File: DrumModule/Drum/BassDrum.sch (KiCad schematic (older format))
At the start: 35 parts, among them J1 Barrel_Jack_Switch, J2 Barrel_Jack_Switch, Q1 MMBT3904, U1 74HC74, U3 LM2904DR, U4 LM2904DR, U5 LM2904DR

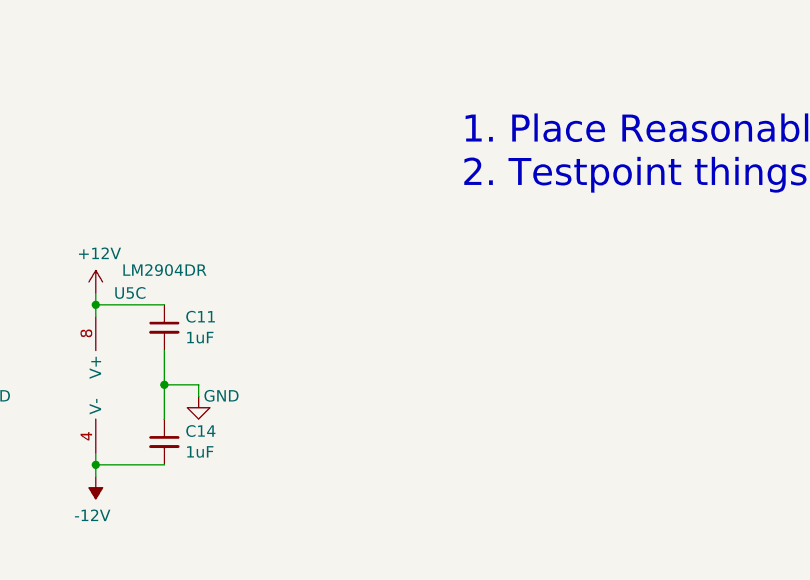
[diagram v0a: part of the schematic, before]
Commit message: Organized layout of drum, should be ready for routing.
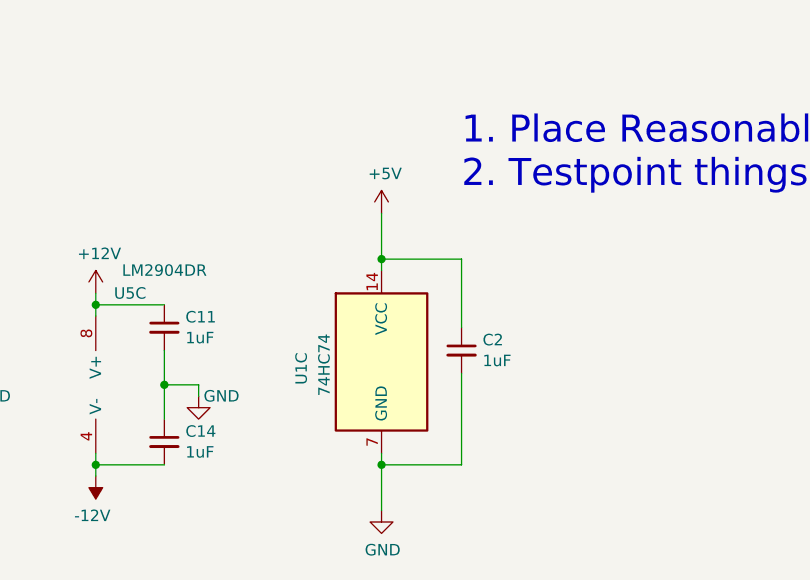
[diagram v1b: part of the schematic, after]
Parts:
- added C2: 1uF, Capacitor_SMD:C_0805_2012Metric, symbol Device:C_Small
- added unit 3 of U1
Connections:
- net +5V: now also C2.1, U1.14 (VCC)
- net GND: now also C2.2, U1.7 (GND)
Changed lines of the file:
@@
 Text Notes 4900 5950 0    118  ~ 0
 1. Place Reasonable values for HPF/LPF.\n2. Testpoint things.
+$Comp
+L 74xx:74HC74 U?
+U 3 1 5C9E2140
+P 4550 6700
+AR Path="/5C9E2140" Ref="U?"  Part="3"
+AR Path="/5C9E40A5/5C9E2140" Ref="U1"  Part="3"
+F 0 "U1" V 4200 6600 50  0000 L CNN
+F 1 "74HC74" V 4300 6550 50  0000 L CNN
+F 2 "Package_SO:SOIC-14_3.9x8.7mm_P1.27mm" H 4550 6700 50  0001 C CNN
+F 3 "74xx/74hc_hct74.pdf" H 4550 6700 50  0001 C CNN
+	3    4550 6700
+	1    0    0    -1
+$EndComp
+Wire Wire Line
+	4550 6300 4550 6250
+Wire Wire Line
+	4550 7100 4550 7150
+$Comp
+L power:GND #PWR?
+U 1 1 5C9E2149
+P 4550 7350
+AR Path="/5C9E2149" Ref="#PWR?"  Part="1"
+AR Path="/5C9E40A5/5C9E2149" Ref="#PWR011"  Part="1"
+F 0 "#PWR011" H 4550 7100 50  0001 C CNN
+F 1 "GND" H 4555 7177 50  0000 C CNN
+F 2 "" H 4550 7350 50  0001 C CNN
+F 3 "" H 4550 7350 50  0001 C CNN
+	1    4550 7350
+	1    0    0    -1
+$EndComp
+Wire Wire Line
+	4550 7150 4900 7150
+Connection ~ 4550 7150
+Wire Wire Line
+	4550 7150 4550 7350
+Wire Wire Line
+	4900 6250 4550 6250
+Connection ~ 4550 6250
+Wire Wire Line
+	4550 6250 4550 6050
+$Comp
+L power:+5V #PWR?
+U 1 1 5C9E2155
+P 4550 6050
+AR Path="/5C9E2155" Ref="#PWR?"  Part="1"
+AR Path="/5C9E40A5/5C9E2155" Ref="#PWR010"  Part="1"
+F 0 "#PWR010" H 4550 5900 50  0001 C CNN
+F 1 "+5V" H 4565 6223 50  0000 C CNN
+F 2 "" H 4550 6050 50  0001 C CNN
+F 3 "" H 4550 6050 50  0001 C CNN
+	1    4550 6050
+	1    0    0    -1
+$EndComp
+$Comp
+L Device:C_Small C?
+U 1 1 5C9E215B
+P 4900 6650
+AR Path="/5C9E215B" Ref="C?"  Part="1"
+AR Path="/5C9E40A5/5C9E215B" Ref="C2"  Part="1"
+F 0 "C2" H 4992 6696 50  0000 L CNN
+F 1 "1uF" H 4992 6605 50  0000 L CNN
+F 2 "Capacitor_SMD:C_0805_2012Metric" H 4900 6650 50  0001 C CNN
+F 3 "~" H 4900 6650 50  0001 C CNN
+	1    4900 6650
+	1    0    0    -1
+$EndComp
+Wire Wire Line
+	4900 6250 4900 6550
+Wire Wire Line
+	4900 6750 4900 7150
 $EndSCHEMATC

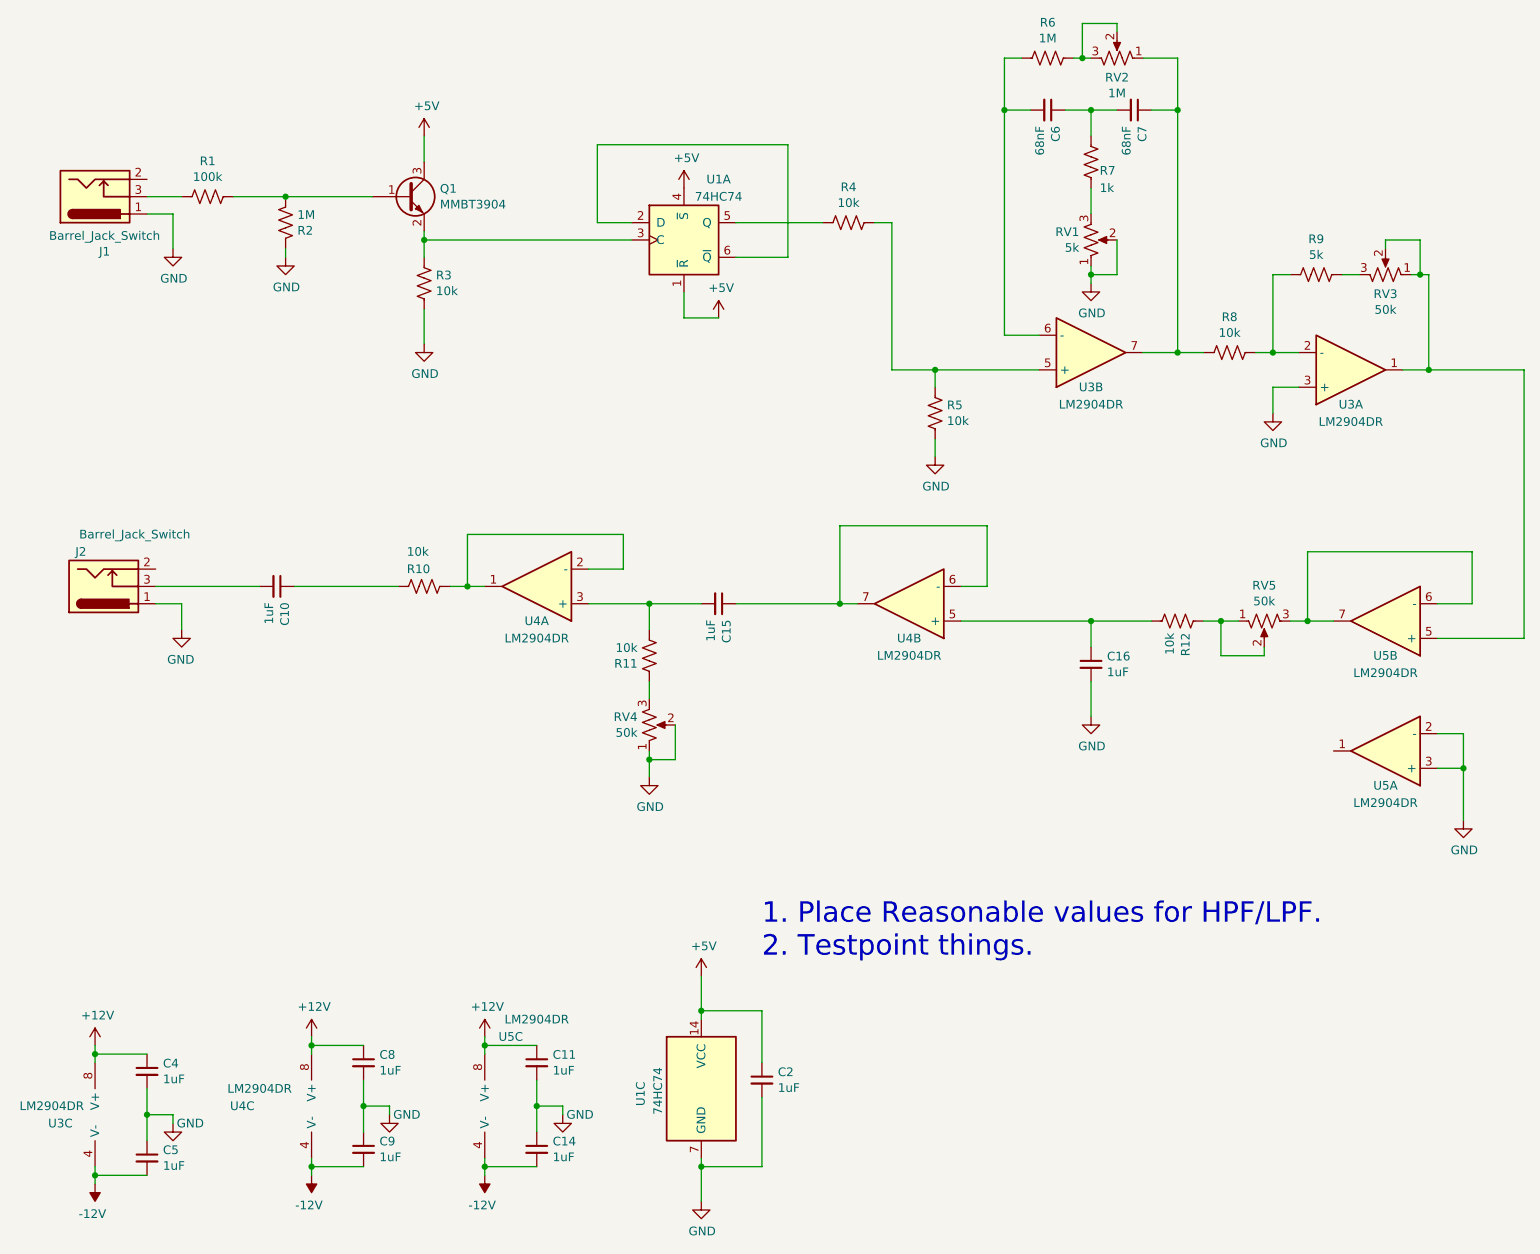
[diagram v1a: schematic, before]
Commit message: locked in filter values
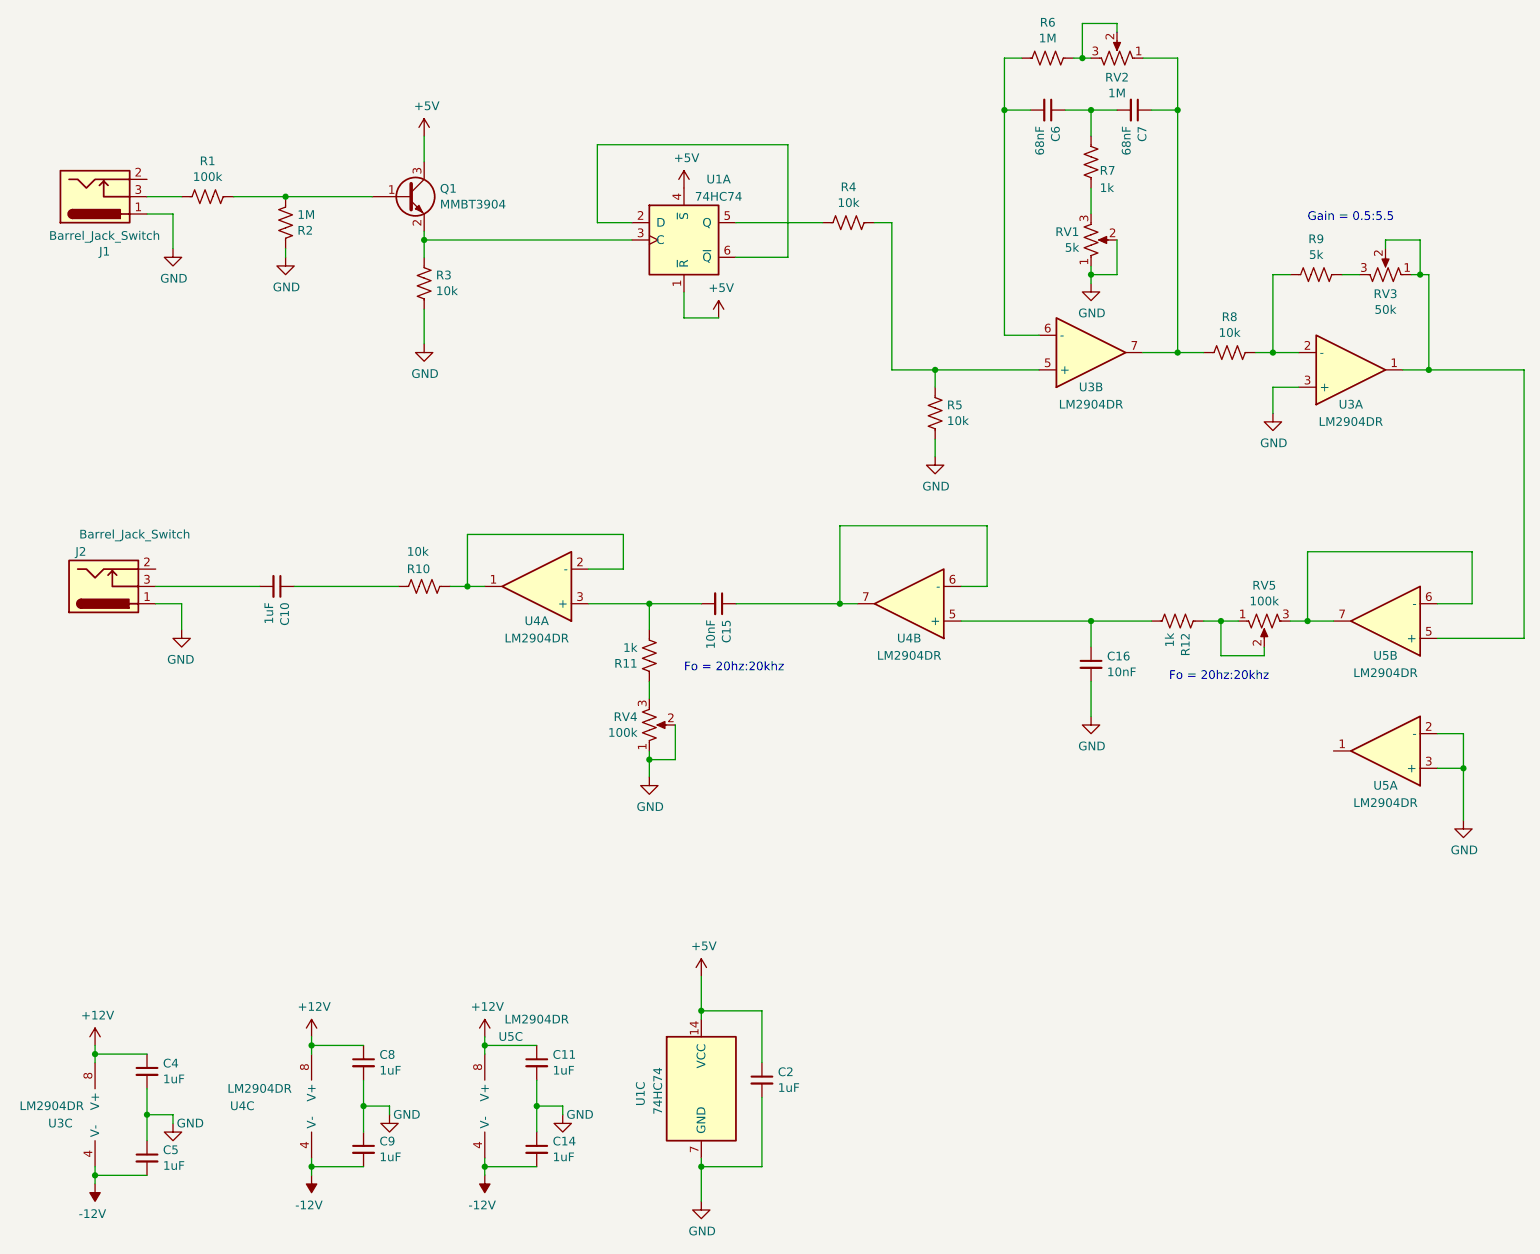
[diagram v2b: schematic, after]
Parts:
- C15, C16: value 1uF -> 10nF
- R11, R12: value 10k -> 1k
- RV4, RV5: value 50k -> 100k
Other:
- note added: "Fo = 20hz:20khz"
- note added: "Gain = 0.5:5.5"
- note removed: "1. Place Reasonable values for HPF/LPF.\n2. Testpoint things."
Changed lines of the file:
@@
 P 7300 4000
 F 0 "R12" H 7368 4046 50  0000 L CNN
-F 1 "10k" H 7368 3955 50  0000 L CNN
+F 1 "1k" H 7368 3955 50  0000 L CNN
 F 2 "Resistor_SMD:R_0805_2012Metric" V 7340 3990 50  0001 C CNN
 F 3 "~" H 7300 4000 50  0001 C CNN
@@
 AR Path="/5C9E40A5/5CA38E3F" Ref="C16"  Part="1"
 F 0 "C16" H 6892 4296 50  0000 L CNN
-F 1 "1uF" H 6892 4205 50  0000 L CNN
+F 1 "10nF" H 6892 4205 50  0000 L CNN
 F 2 "Capacitor_SMD:C_0805_2012Metric" H 6800 4250 50  0001 C CNN
 F 3 "~" H 6800 4250 50  0001 C CNN
@@
 P 4250 4200
 F 0 "R11" H 4318 4246 50  0000 L CNN
-F 1 "10k" H 4318 4155 50  0000 L CNN
+F 1 "1k" H 4318 4155 50  0000 L CNN
 F 2 "Resistor_SMD:R_0805_2012Metric" V 4290 4190 50  0001 C CNN
 F 3 "~" H 4250 4200 50  0001 C CNN
@@
 AR Path="/5C9E40A5/5CA4B038" Ref="C15"  Part="1"
 F 0 "C15" H 4742 3946 50  0000 L CNN
-F 1 "1uF" H 4742 3855 50  0000 L CNN
+F 1 "10nF" H 4742 3855 50  0000 L CNN
 F 2 "Capacitor_SMD:C_0805_2012Metric" H 4650 3900 50  0001 C CNN
 F 3 "~" H 4650 3900 50  0001 C CNN
@@
 P 4250 4600
 F 0 "RV4" H 4182 4554 50  0000 R CNN
-F 1 "50k" H 4182 4645 50  0000 R CNN
+F 1 "100k" H 4182 4645 50  0000 R CNN
 F 2 "Eurocad:Alpha9mmPot" H 4250 4600 50  0001 C CNN
 F 3 "~" H 4250 4600 50  0001 C CNN
@@
 P 7800 4000
 F 0 "RV5" V 7595 4000 50  0000 C CNN
-F 1 "50k" V 7686 4000 50  0000 C CNN
+F 1 "100k" V 7686 4000 50  0000 C CNN
 F 2 "Eurocad:Alpha9mmPot" H 7800 4000 50  0001 C CNN
 F 3 "~" H 7800 4000 50  0001 C CNN
@@
 	3300 7200 3300 7150
 Connection ~ 3300 7150
-Text Notes 4900 5950 0    118  ~ 0
-1. Place Reasonable values for HPF/LPF.\n2. Testpoint things.
 $Comp
 L 74xx:74HC74 U?
@@
 Wire Wire Line
 	4900 6750 4900 7150
+Text Notes 8050 1700 0    50   ~ 0
+Gain = 0.5:5.5
+Text Notes 7250 4350 0    50   ~ 0
+Fo = 20hz:20khz
+Text Notes 4450 4300 0    50   ~ 0
+Fo = 20hz:20khz
 $EndSCHEMATC

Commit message: Forgot to save
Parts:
- RV1: value 5k -> 1k
- RV2: value 1M -> 100k
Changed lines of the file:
@@
 P 6800 1800
 F 0 "RV1" H 6732 1754 50  0000 R CNN
-F 1 "5k" H 6732 1845 50  0000 R CNN
+F 1 "1k" H 6732 1845 50  0000 R CNN
 F 2 "Eurocad:Alpha9mmPot" H 6800 1800 50  0001 C CNN
 F 3 "~" H 6800 1800 50  0001 C CNN
@@
 P 6950 750
 F 0 "RV2" V 6838 750 50  0000 C CNN
-F 1 "1M" V 6747 750 50  0000 C CNN
+F 1 "100k" V 6747 750 50  0000 C CNN
 F 2 "Eurocad:Alpha9mmPot" H 6950 750 50  0001 C CNN
 F 3 "~" H 6950 750 50  0001 C CNN

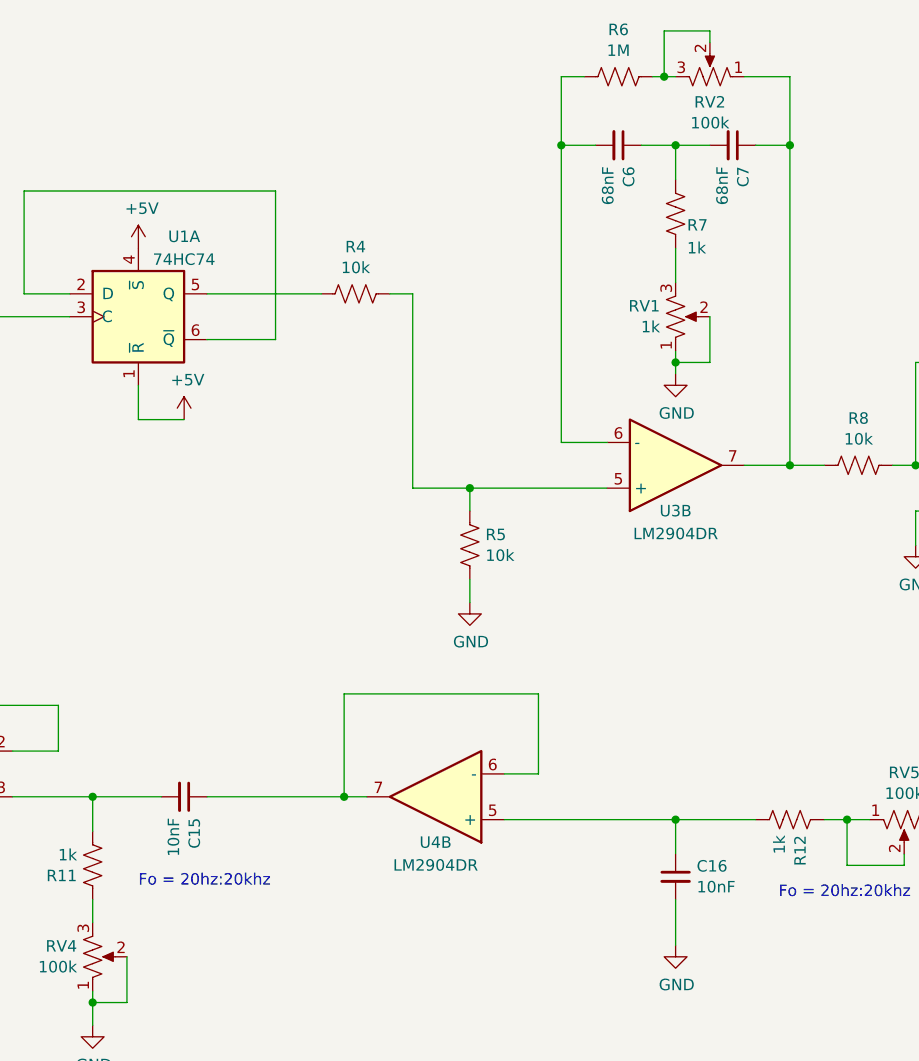
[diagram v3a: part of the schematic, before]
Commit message: Updated parts for the Bob bass
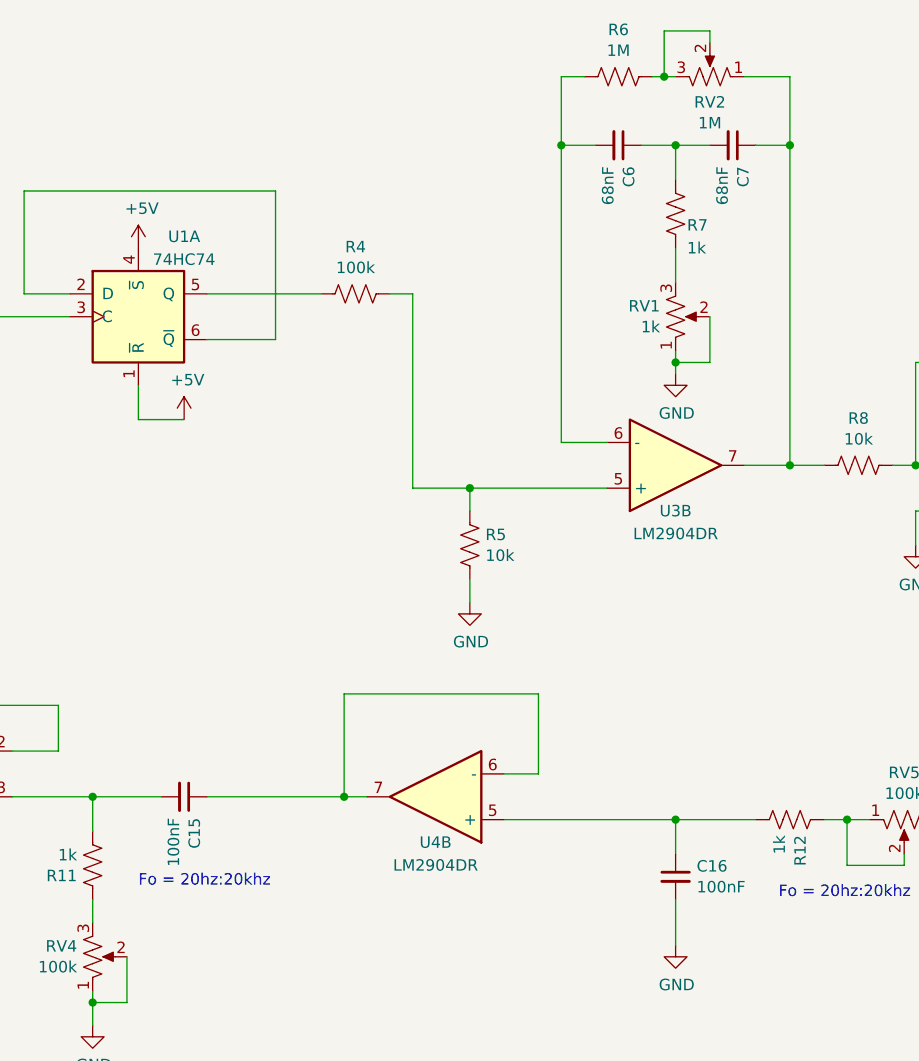
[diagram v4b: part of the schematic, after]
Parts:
- C15, C16: value 10nF -> 100nF
- R4: value 10k -> 100k
- RV2: value 100k -> 1M
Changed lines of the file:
@@
 P 5400 1700
 F 0 "R4" V 5605 1700 50  0000 C CNN
-F 1 "10k" V 5514 1700 50  0000 C CNN
+F 1 "100k" V 5514 1700 50  0000 C CNN
 F 2 "Resistor_SMD:R_0805_2012Metric" V 5440 1690 50  0001 C CNN
 F 3 "~" H 5400 1700 50  0001 C CNN
@@
 P 6950 750
 F 0 "RV2" V 6838 750 50  0000 C CNN
-F 1 "100k" V 6747 750 50  0000 C CNN
+F 1 "1M" V 6747 750 50  0000 C CNN
 F 2 "Eurocad:Alpha9mmPot" H 6950 750 50  0001 C CNN
 F 3 "~" H 6950 750 50  0001 C CNN
@@
 AR Path="/5C9E40A5/5CA38E3F" Ref="C16"  Part="1"
 F 0 "C16" H 6892 4296 50  0000 L CNN
-F 1 "10nF" H 6892 4205 50  0000 L CNN
+F 1 "100nF" H 6892 4205 50  0000 L CNN
 F 2 "Capacitor_SMD:C_0805_2012Metric" H 6800 4250 50  0001 C CNN
 F 3 "~" H 6800 4250 50  0001 C CNN
@@
 AR Path="/5C9E40A5/5CA4B038" Ref="C15"  Part="1"
 F 0 "C15" H 4742 3946 50  0000 L CNN
-F 1 "10nF" H 4742 3855 50  0000 L CNN
+F 1 "100nF" H 4742 3855 50  0000 L CNN
 F 2 "Capacitor_SMD:C_0805_2012Metric" H 4650 3900 50  0001 C CNN
 F 3 "~" H 4650 3900 50  0001 C CNN
